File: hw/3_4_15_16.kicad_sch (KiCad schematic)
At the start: 9 parts, among them U13 ATmega2560-16A, U14 MIC5504-3.3YM5, U15 bmx055, U16 bmx055

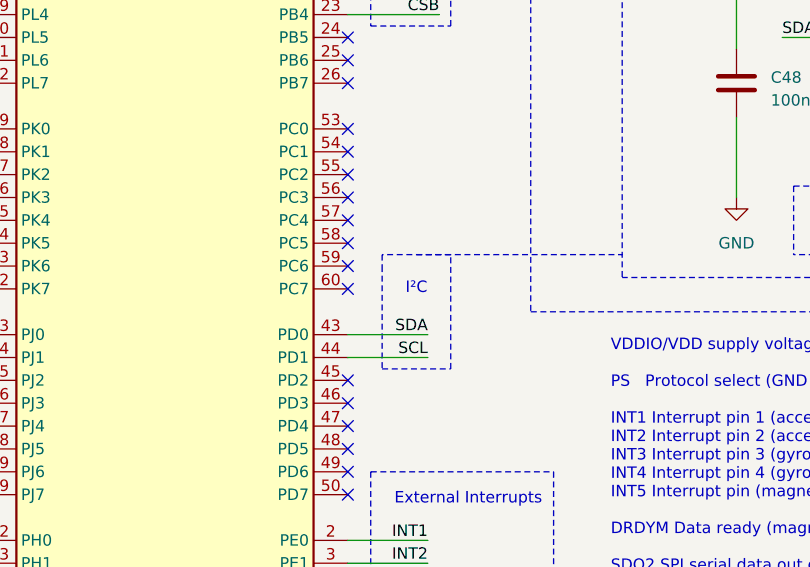
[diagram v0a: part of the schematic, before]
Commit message: Add LM2576S-5 to 2.3.10
Signed-off-by: ckalina <46683072+ckalina@users.noreply.github.com>
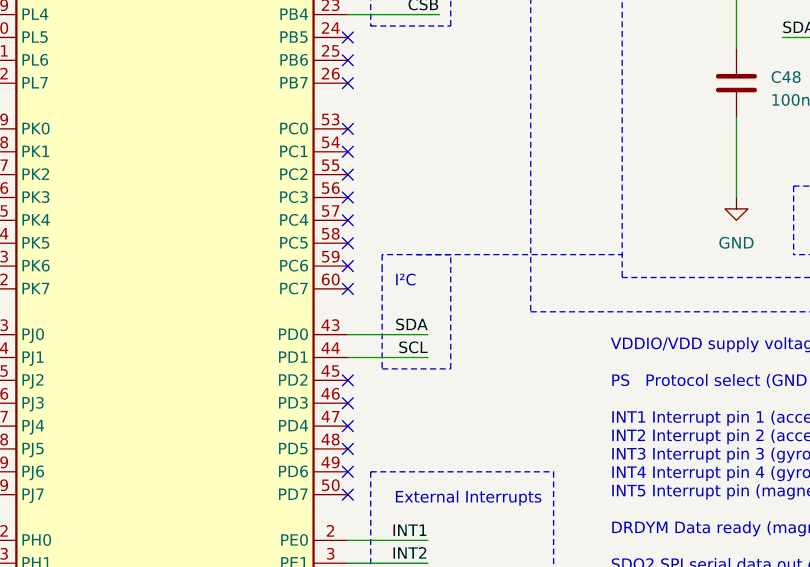
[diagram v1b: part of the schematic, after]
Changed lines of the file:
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@@
   )
   (text "I²C" (at 72.39 114.3 180)
-    (effects (font (size 1.27 1.27)))
+    (effects (font (size 1.27 1.27)) (justify right bottom))
   )
   (text "External Interrupts" (at 86.36 138.43 180)
